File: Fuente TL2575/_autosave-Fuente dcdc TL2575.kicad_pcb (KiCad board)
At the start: 2 copper layers, 55.9 x 38.1 mm, 23 parts, among them U1 TL2575

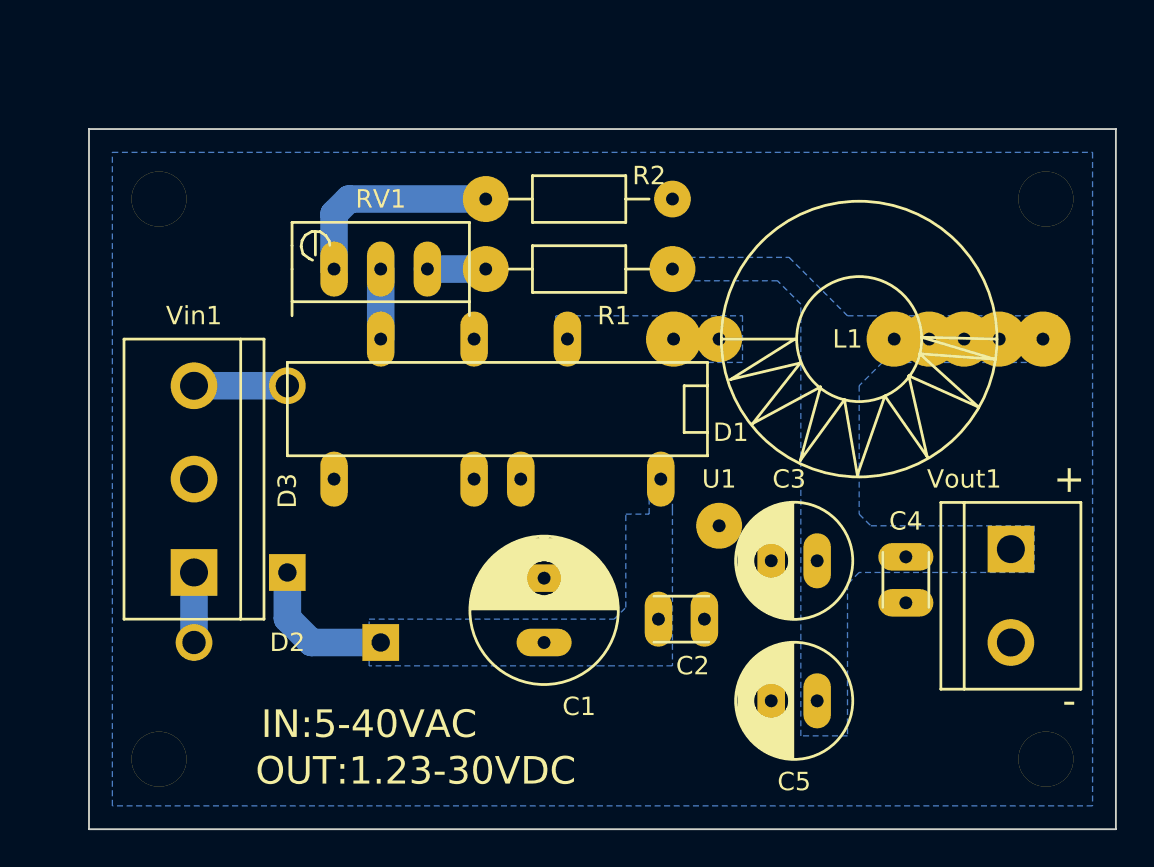
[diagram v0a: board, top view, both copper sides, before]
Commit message: Se realizó la segunda versión de la fuente TL2575
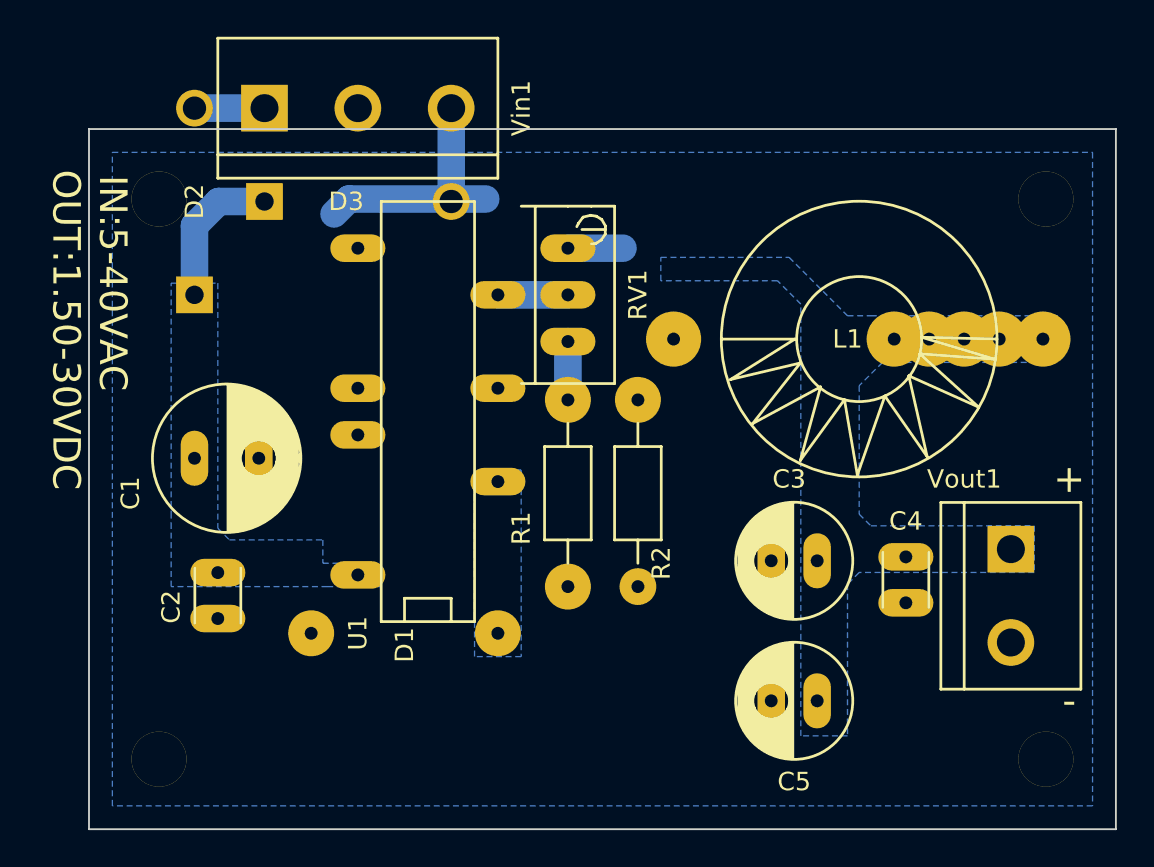
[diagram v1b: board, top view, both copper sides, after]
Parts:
- moved D2 24.5 mm to (103.5, 40.8), turned to 270 degrees
- moved C2 24.1 mm to (104.8, 61.0), turned to 270 degrees
- moved Vin1 22.1 mm to (112.4, 35.7), turned to 0 degrees
- moved C1 21.5 mm to (103.5, 54.7), turned to 0 degrees
- moved D1 20.3 mm to (115.0, 64.3), turned to 0 degrees
- moved R2 16.3 mm to (127.7, 56.6), turned to 270 degrees
- moved D3 15.6 mm to (112.4, 40.8), turned to 180 degrees
- moved RV1 12.8 mm to (123.9, 43.3), turned to 180 degrees
- moved R1 12.2 mm to (123.9, 56.6), turned to 90 degrees
- moved U1 3.79 mm to (116.2, 52.2), turned to 90 degrees
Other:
- board text added: "OUT:1.50-30VDC"
- board text removed: "OUT:1.23-30VDC"
